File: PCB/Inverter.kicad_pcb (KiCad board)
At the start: 2 copper layers, 71.9 x 99.1 mm, 79 parts, among them J1 Conn_01x02, J2 Conn_01x05_Pin, J3 Conn_01x05_Pin, Q1 STP110N8F6, Q2 STP110N8F6, Q3 STP110N8F6, Q4 STP110N8F6, Q5 STP110N8F6, Q6 STP110N8F6, U1 XL7015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

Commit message: Change#012
The outputs on the board for setting the operation of half-bridges have been changed, as well as the inputs for Hall sensors, so that they are in the space of one port and read by one line of code, and the interrupts for level changes in the code have been changed to accommodate this feature.
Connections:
- A1 pad 10: /IN_V -> /HAL_W
- A1 pad 14: /HAL_W -> /IN_V
- A1 pad 15: /HAL_V -> /IN_W
- A1 pad 9: /IN_W -> /HAL_V
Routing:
- net /IN_W: track 57.3 -> 73.1 mm, vias 1 -> 2
- net /HAL_V: track 27.1 -> 13.5 mm, vias 0 -> 2
- net /HAL_W: track 27.1 -> 17.1 mm
- net /IN_V: track 51.6 -> 56.3 mm, vias 1 -> 2
- net /POT: track 49.0 -> 51.8 mm
- net /CWR: track 46.8 -> 45.1 mm
- net /IN_U: track 43.3 -> 42.0 mm
- net /PWM_V: track 52.1 -> 53.0 mm
- net +5V_Fuse: track 65.3 -> 65.8 mm, vias 5 -> 3
- net GND: vias 278 -> 279

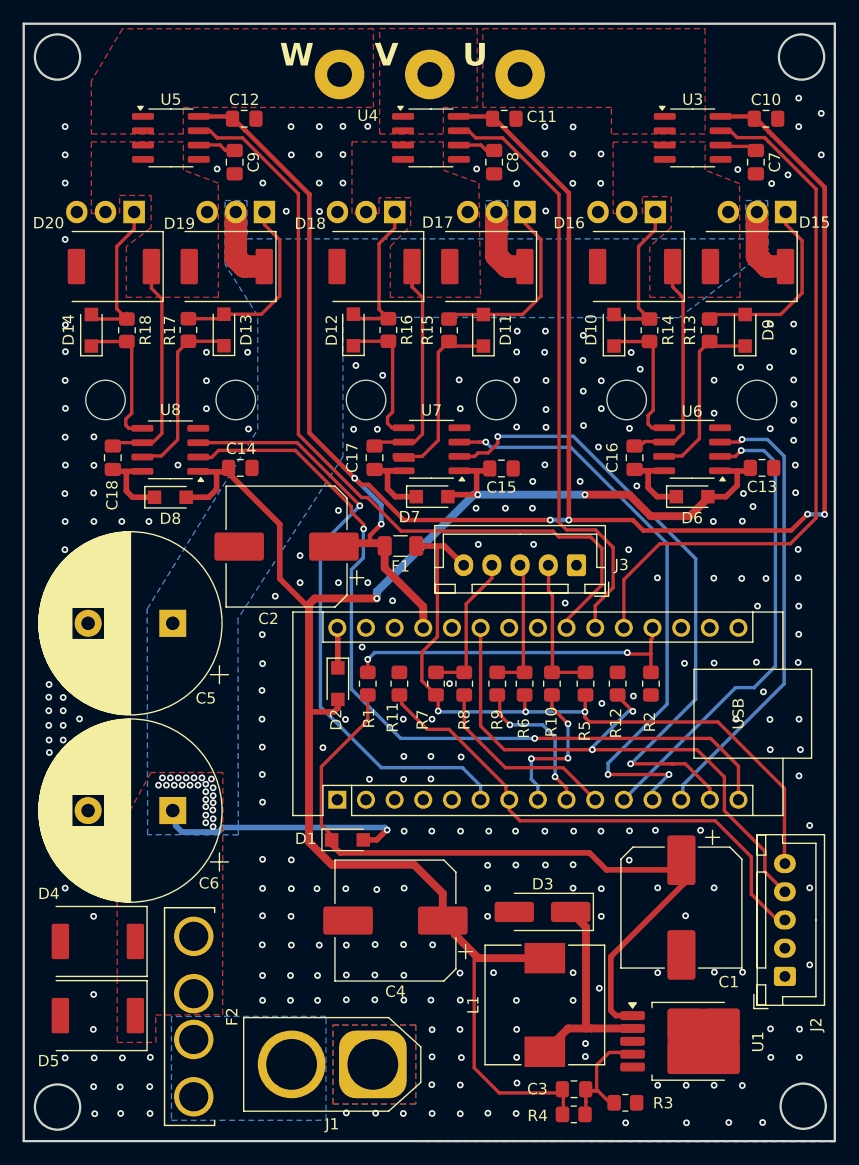
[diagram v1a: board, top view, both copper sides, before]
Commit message: Change#014
Added capacitors for the outputs from the Hall sensors.
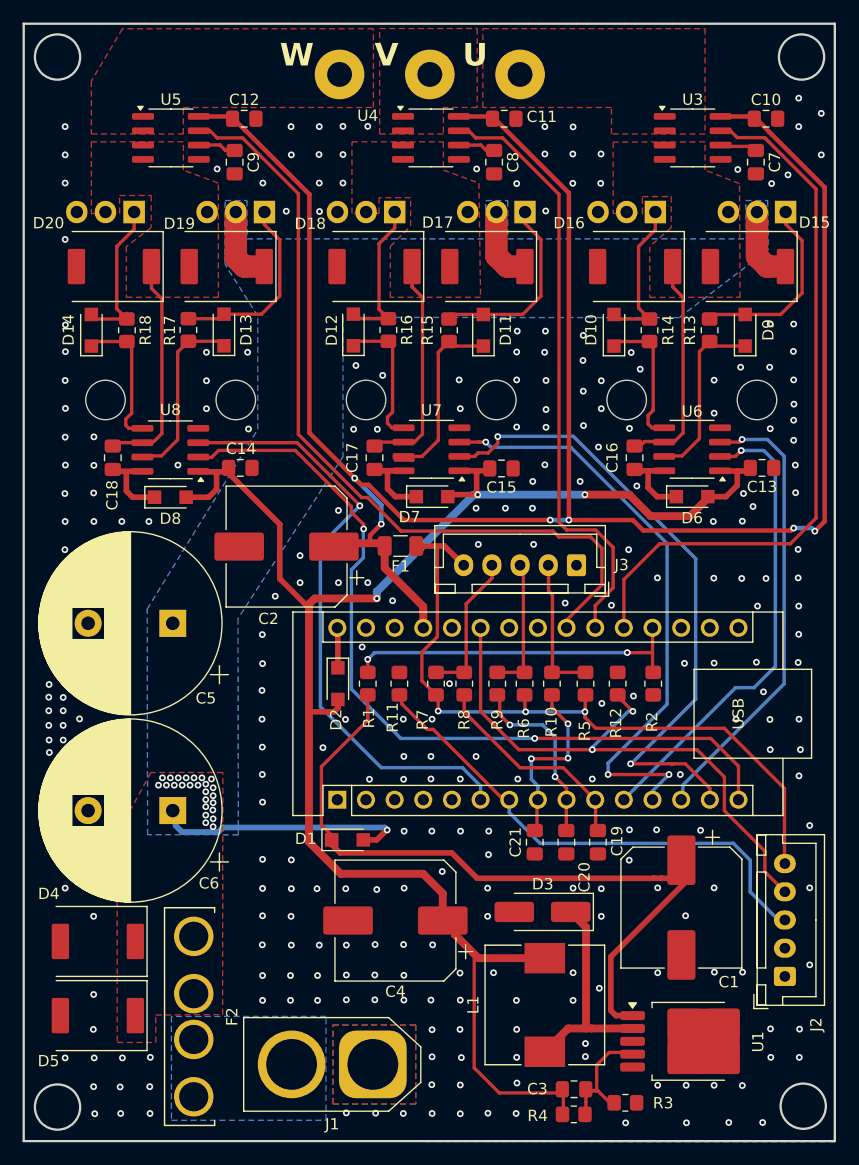
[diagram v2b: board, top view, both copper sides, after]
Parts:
- added C19: 1nF, Capacitor_SMD:C_0805_2012Metric_Pad1.18x1.45mm_HandSolder, F.Cu at (154.7, 115.9)
- added C20: 1nF, Capacitor_SMD:C_0805_2012Metric_Pad1.18x1.45mm_HandSolder, F.Cu at (151.9, 115.9)
- added C21: 1nF, Capacitor_SMD:C_0805_2012Metric_Pad1.18x1.45mm_HandSolder, F.Cu at (149.1, 115.9)
- R5, R6, R7: value 10K -> 1K
- moved R2 0.20 mm to (159.6, 101.9)
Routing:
- net /HAL_U: track 13.3 -> 16.1 mm
- net /HAL_V: track 13.5 -> 16.3 mm
- net /HAL_W: track 17.1 -> 19.1 mm
- net /POT: track 51.8 -> 51.0 mm
- net +5V: track 188.1 -> 188.7 mm
- net GND: vias 279 -> 278
